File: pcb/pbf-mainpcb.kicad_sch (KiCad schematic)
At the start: 66 parts, among them J1 USB_B_Micro, J2 Conn_01x02_Female, J3 Conn_01x02_Female, J4 Conn_01x03_Female, J5 Conn_01x05_Female, J6 Conn_01x04_Female, J7 Conn_01x10_Female, Q1 AO3401, SW1 SW_SPDT, U1 TCA9534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

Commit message: Fix things I bodged in my prototype
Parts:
- added D5: 12V zener, Diode_SMD:D_MELF, symbol Device:D_Zener
- added R18: 10K, Resistor_SMD:R_0603_1608Metric, symbol Device:R
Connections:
- net GND: now also D5.2 (A)
- net MLCD_A: now also D5.1 (K)
- net at R2.2, U3.4 (-IN): now also R18.1
- net at J2.1 (Pin_1), U3.5 (VO1): now also R18.2
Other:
- note added: "Want: ESP32-S3-WROOM-1- (N8R2 or N16R2) Quad RAM works well enough and we need the GPIOs that would otherwise be occupied by octal PSRAM"
- note removed: "Backlight: Vfw=2.9-3.1V Ibl=45-60mA"
- note removed: "GPIO26-37 NC because octal PSRAM"
- note removed: "Want: ESP32-S3-WROOM-1-NxR8 (Or not? Quad RAM seems to be sufficient and we need all GPIOs we can spare)"
- moved on the sheet: C3, C4, R2

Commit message: added readme description, changed zener 12V -> 15V
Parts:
- D5: value 12V zener -> 15V zener

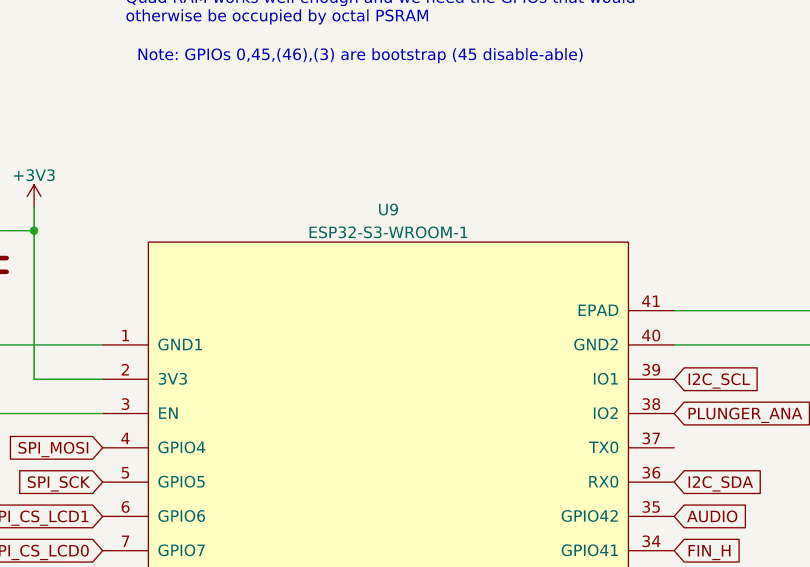
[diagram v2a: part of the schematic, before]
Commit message: Make it more clearer that you cannot use octal psram
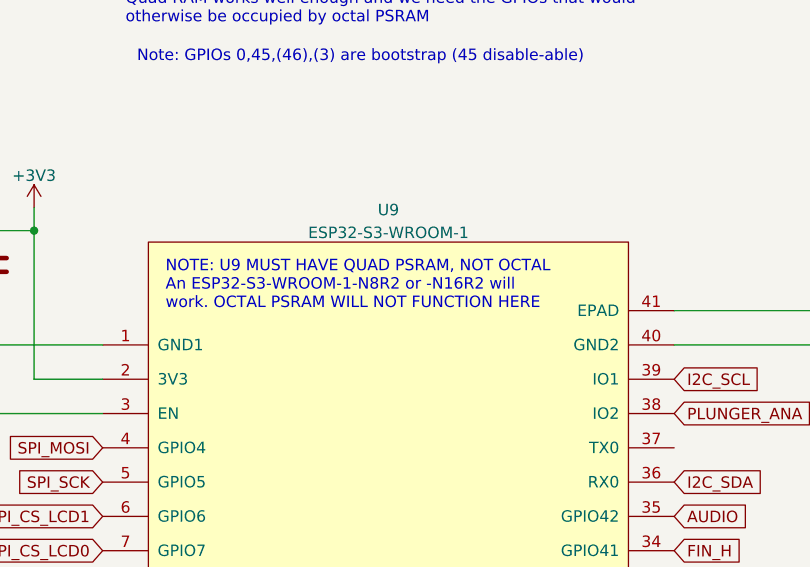
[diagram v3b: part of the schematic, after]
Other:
- note added: "NOTE: U9 MUST HAVE QUAD PSRAM, NOT OCTAL An ESP32-S3-WROOM-1-N8R2 or -N16R2 will work. OCTAL PSRAM WILL NOT FUNCTION HERE"
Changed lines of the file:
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@@
+    (effects (font (size 1.27 1.27)) (justify left bottom))
+  )
+  (text "NOTE: U9 MUST HAVE QUAD PSRAM, NOT OCTAL\nAn ESP32-S3-WROOM-1-N8R2 or -N16R2 will\nwork. OCTAL PSRAM WILL NOT FUNCTION HERE"
+    (at 230.505 73.66 0)
     (effects (font (size 1.27 1.27)) (justify left bottom))
   )
